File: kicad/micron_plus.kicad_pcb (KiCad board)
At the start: 2 copper layers, 163.8 x 123.2 mm, 90 parts, among them J1 Conn_02x17_Odd_Even, J2 Cliff DC10A, Q1 2N2905A, Q2 2N2905A, Q3 2N3904, Q4 2N3904, U1 MC68A21, U10 74LS00, U11 7406, U12 HM6264LP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

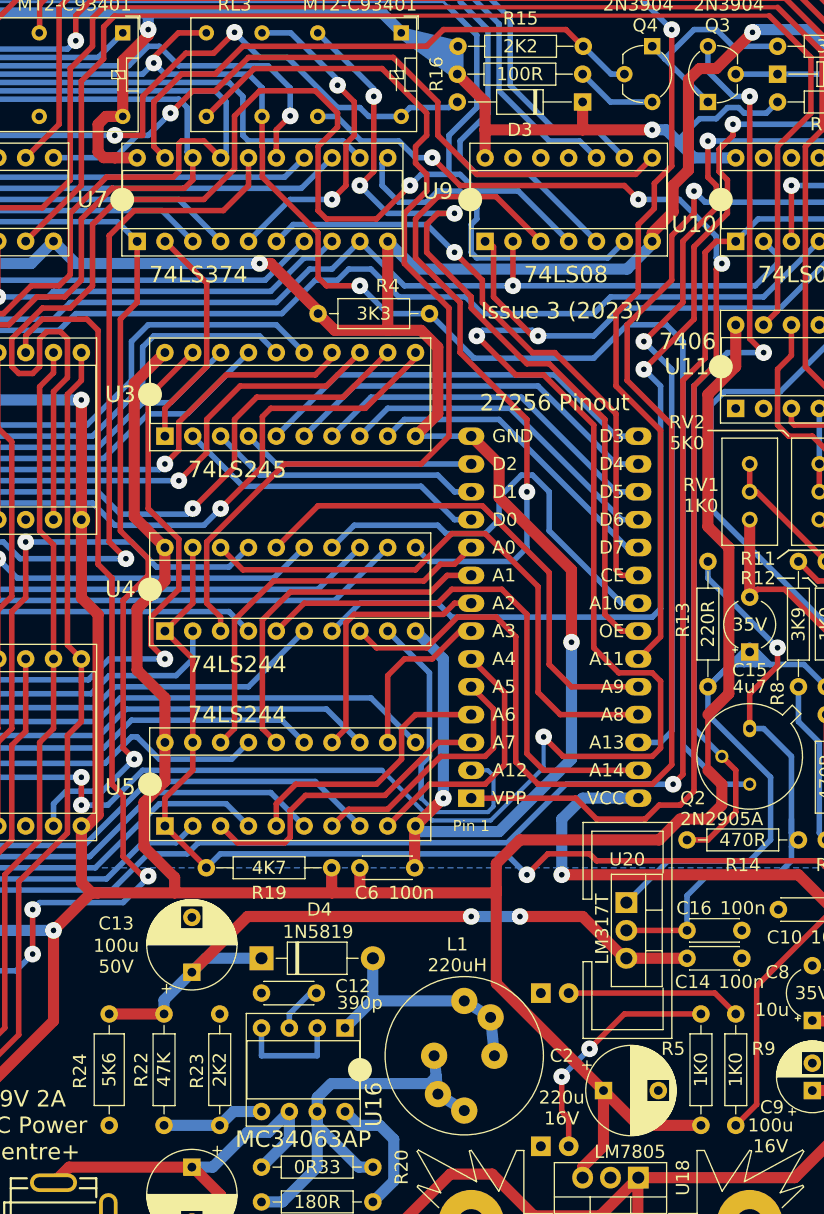
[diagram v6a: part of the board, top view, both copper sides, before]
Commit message: KiCAD: larger footprint for 1W resistors
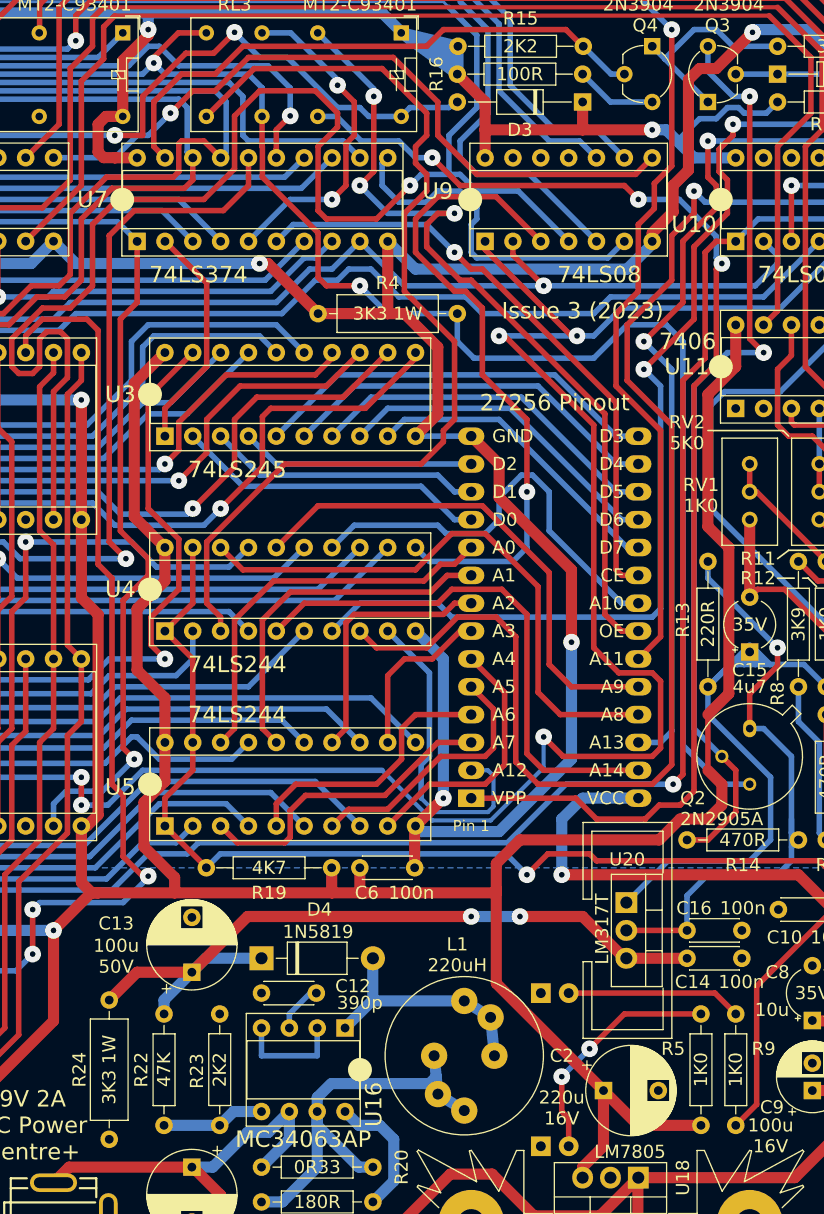
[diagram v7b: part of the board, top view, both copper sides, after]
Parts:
- R24: value 5K6 -> 3K3 1W; footprint Resistor_THT:R_Axial_DIN0207_L6.3mm_D2.5mm_P10.16mm_Horizontal -> Resistor_THT:R_Axial_DIN0309_L9.0mm_D3.2mm_P12.70mm_Horizontal
- R4: value 3K3 -> 3K3 1W; footprint Resistor_THT:R_Axial_DIN0207_L6.3mm_D2.5mm_P10.16mm_Horizontal -> Resistor_THT:R_Axial_DIN0309_L9.0mm_D3.2mm_P12.70mm_Horizontal
- moved R4 2.54 mm to (158.8, 54.9)
- moved R24 1.27 mm to (127.0, 130.2)
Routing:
- net /Power Supply/28VDC: track 65.6 -> 69.2 mm
- net /1MHz Bus and PIA Interface/Addr12: track 289.6 -> 286.7 mm
- net /Main Logic and Eprom Socket/EpromVPP: track 181.0 -> 182.5 mm
- net GND: track 678.0 -> 676.6 mm
- net /Control Latches/n2564Mode: track 126.7 -> 127.9 mm
- net /Main Logic and Eprom Socket/Eprom22VPP: track 76.4 -> 75.8 mm
- net /Control Latches/Eprom20: track 56.4 -> 55.8 mm
- net Net-(U4-Pad11): track 59.3 -> 59.9 mm

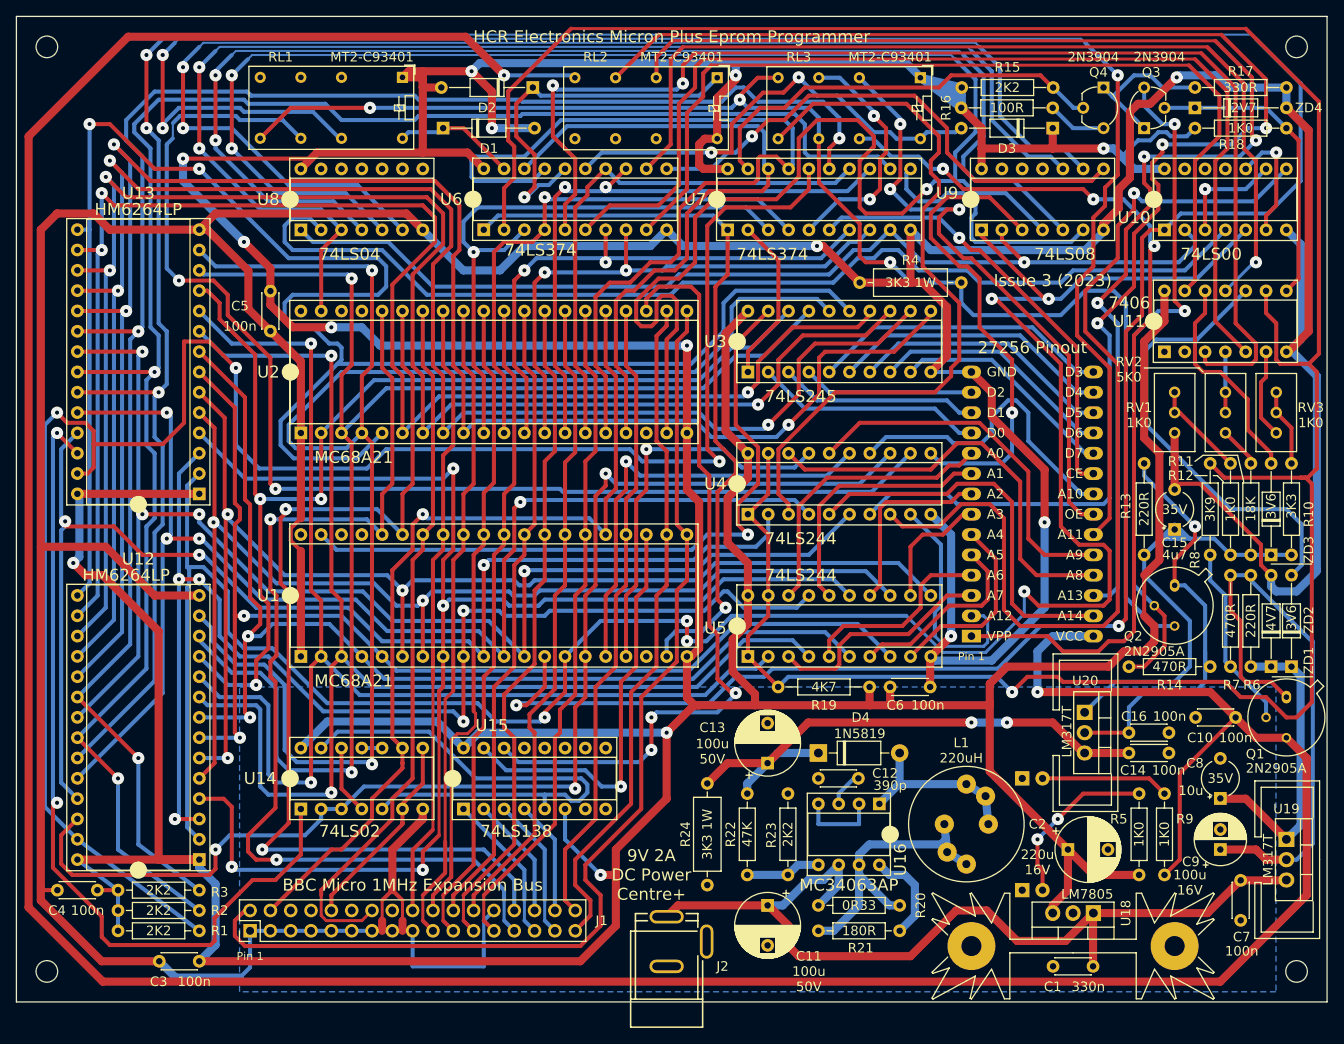
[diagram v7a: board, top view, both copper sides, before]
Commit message: KiCAD: Make space for full ZIF
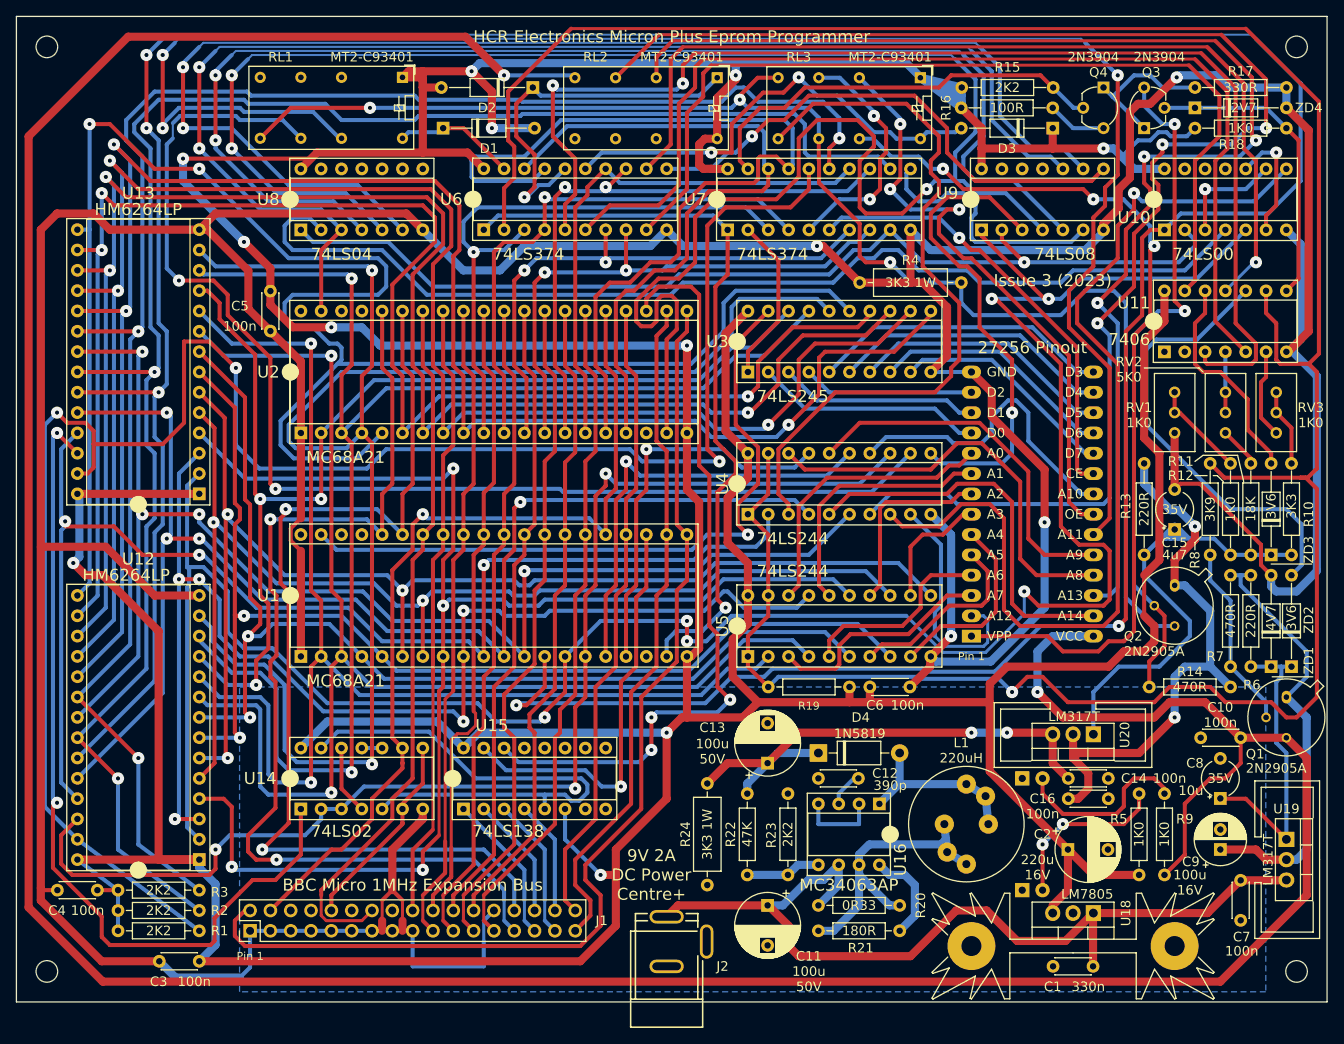
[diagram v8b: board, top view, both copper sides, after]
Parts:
- R19: footprint custom_footprints:R_Axial_DIN0207_L6.3mm_D2.0mm_P11.43mm_Horizontal -> custom_footprints:R_Axial_DIN0207_L6.3mm_D2.0mm_P10.16mm_Horizontal
- U17: footprint custom_footprints:DIP-28_W15.24mm_Socket_LongPads -> custom_footprints:DIP_Socket-28_W11.9_W12.7_W15.24_W17.78_W18.5_3M_228-1277-00-0602J
- U3, U4, U5: footprint custom_footprints:DIP-20_W7.62mm_Socket -> custom_footprints:DIP-20_W7.62mm_Socket_tweaked
- moved C16 11.2 mm to (172.1, 119.4)
- moved C14 8.22 mm to (172.1, 116.8)
- moved R14 3.59 mm to (192.4, 105.4)
- moved HS3 2.95 mm to (175.3, 111.3), turned to 180 degrees
- moved U20 2.95 mm to (175.3, 111.3), turned to 180 degrees
- moved C10 2.62 mm to (193.7, 111.8)
- moved C6 2.54 mm to (147.3, 105.4)
- moved R19 2.51 mm to (144.8, 105.4)
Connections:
- net Net-(C16-Pad1) renamed /Power Supply/EpromVPPUnswitched
- net Net-(C9-Pad1) renamed /Power Supply/EpromVCCUnswitched
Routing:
- net /Power Supply/EpromVCCUnswitched: track 72.3 -> 54.2 mm
- net /Power Supply/EpromVPPUnswitched: track 55.9 -> 71.3 mm, vias 1 -> 2
- net Net-(LED2-Pad2): track 16.0 -> 22.5 mm
- net /Power Supply/28VDC: track 69.2 -> 63.7 mm
- net /Control Latches/nVCCEnable: track 335.9 -> 338.8 mm
- net GND: track 676.6 -> 677.7 mm
- net Net-(C15-Pad1): track 65.0 -> 65.9 mm
- net /1MHz Bus and PIA Interface/nCSPIA2: track 96.9 -> 96.0 mm
- net /Main Logic and Eprom Socket/Eprom23VPP: track 218.3 -> 219.2 mm
- net Net-(U10-Pad8): track 121.7 -> 122.5 mm
- net /1MHz Bus and PIA Interface/Data5: track 203.9 -> 204.7 mm
- net VCC: track 825.9 -> 825.2 mm
